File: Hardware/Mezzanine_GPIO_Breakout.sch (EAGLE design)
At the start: 12 parts, among them U2 EDISON_CONNECTOR_FULLMOUNTING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, U3 EDISON_CONNECTOR_FULLHEADER

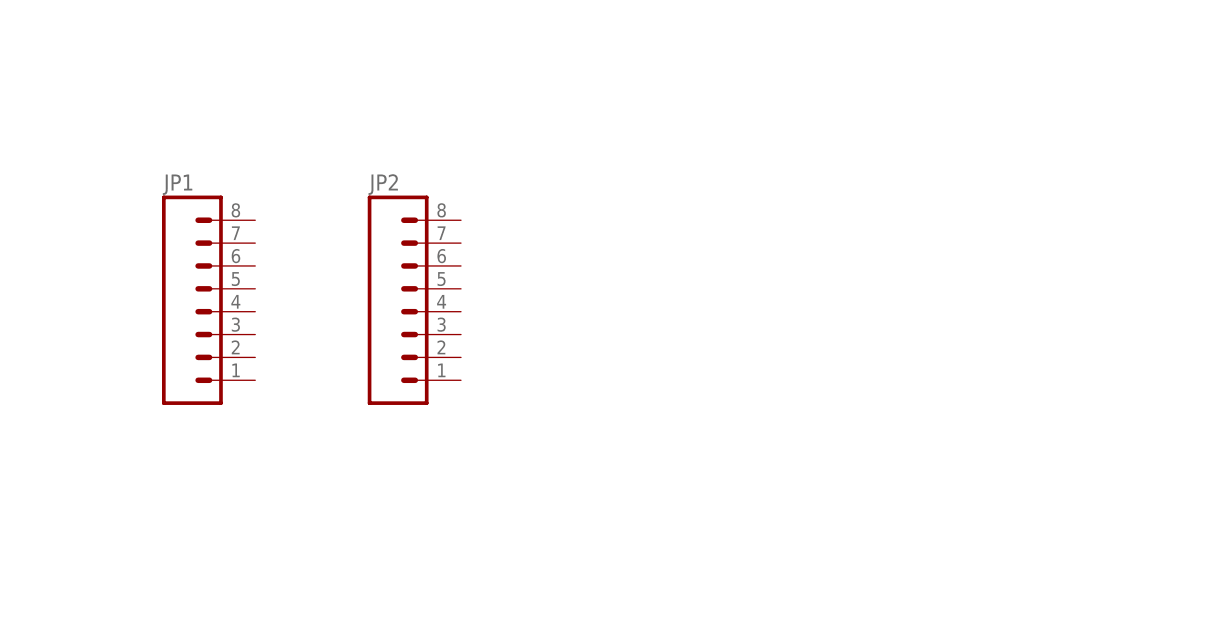
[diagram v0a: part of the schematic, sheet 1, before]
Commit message: completed layout of GPIO Ready for review
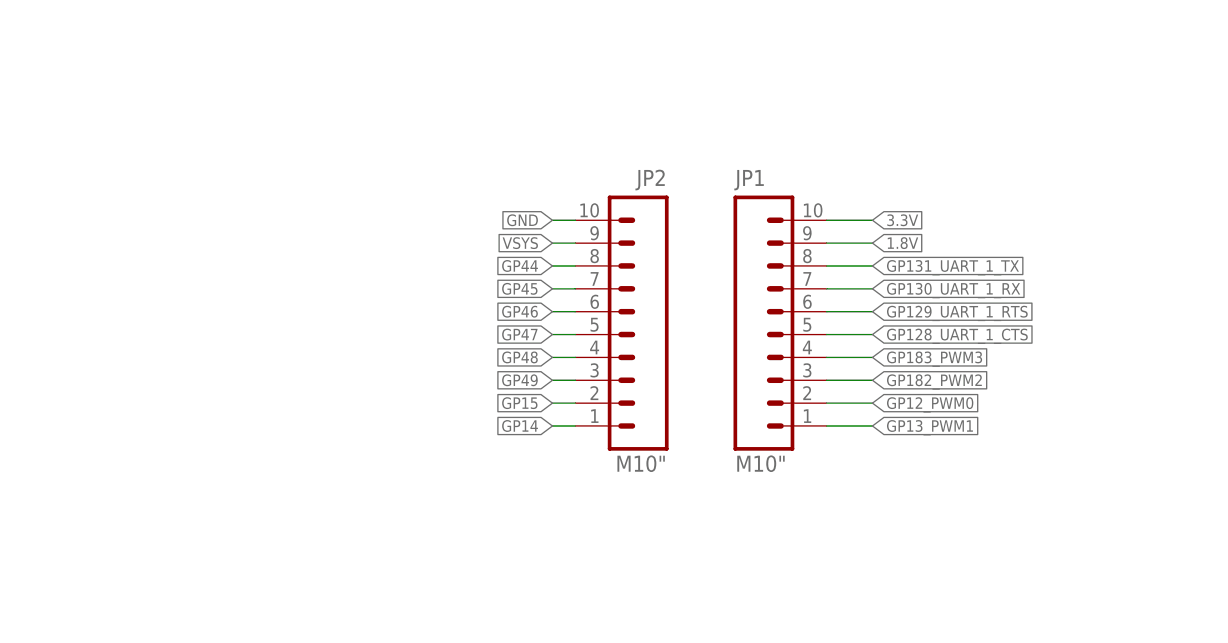
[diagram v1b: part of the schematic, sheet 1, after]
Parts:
- JP1, JP2: value (none) -> M10"; device SparkFun-Connectors:M08 -> SparkFun-Connectors:M10"
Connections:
- net 1.8V: now also JP1.9
- net 3.3V: now also JP1.10
- net GND: now also JP2.10
- net GP128_UART_1_CTS: now also JP1.5
- net GP129_UART_1_RTS: now also JP1.6
- net GP12_PWM0: now also JP1.2
- net GP130_UART_1_RX: now also JP1.7
- net GP131_UART_1_TX: now also JP1.8
- net GP13_PWM1: now also JP1.1
- net GP14: now also JP2.1
- net GP15: now also JP2.2
- net GP182_PWM2: now also JP1.3
- net GP183_PWM3: now also JP1.4
- net GP44: now also JP2.8
- net GP45: now also JP2.7
- net GP46: now also JP2.6
- net GP47: now also JP2.5
- net GP48: now also JP2.4
- net GP49: now also JP2.3
- net VSYS: now also JP2.9
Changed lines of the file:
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@@
 <part name="FID3" library="SparkFun-Aesthetics" deviceset="FIDUCIAL" device="1X2"/>
 <part name="FID4" library="SparkFun-Aesthetics" deviceset="FIDUCIAL" device="1X2"/>
-<part name="JP1" library="SparkFun-Connectors" deviceset="M08" device=""/>
-<part name="JP2" library="SparkFun-Connectors" deviceset="M08" device=""/>
+<part name="JP1" library="SparkFun-Connectors" deviceset="M10" device="&quot;"/>
+<part name="JP2" library="SparkFun-Connectors" deviceset="M10" device="&quot;"/>
 </parts>
 <sheets>
@@
 <instance part="FID3" gate="G$1" x="241.3" y="30.48"/>
 <instance part="FID4" gate="G$1" x="246.38" y="30.48"/>
-<instance part="JP1" gate="G$1" x="68.58" y="101.6"/>
-<instance part="JP2" gate="G$1" x="91.44" y="101.6"/>
+<instance part="JP1" gate="G$1" x="127" y="106.68"/>
+<instance part="JP2" gate="G$1" x="119.38" y="106.68" rot="MR0"/>
 </instances>
 <busses>
 </busses>
 <nets>
+<net name="GP14" class="0">
+<segment>
+<wire x1="109.22" y1="88.9" x2="106.68" y2="88.9" width="0.1524" layer="91"/>
+<label x="106.68" y="88.9" size="1.27" layer="95" rot="R180" xref="yes"/>
+<pinref part="JP2" gate="G$1" pin="1"/>
+</segment>
+</net>
+<net name="GP15" class="0">
+<segment>
+<wire x1="109.22" y1="91.44" x2="106.68" y2="91.44" width="0.1524" layer="91"/>
+<label x="106.68" y="91.44" size="1.27" layer="95" rot="R180" xref="yes"/>
+<pinref part="JP2" gate="G$1" pin="2"/>
+</segment>
+</net>
+<net name="GP49" class="0">
+<segment>
+<wire x1="109.22" y1="93.98" x2="106.68" y2="93.98" width="0.1524" layer="91"/>
+<label x="106.68" y="93.98" size="1.27" layer="95" rot="R180" xref="yes"/>
+<pinref part="JP2" gate="G$1" pin="3"/>
+</segment>
+</net>
+<net name="GP48" class="0">
+<segment>
+<wire x1="109.22" y1="96.52" x2="106.68" y2="96.52" width="0.1524" layer="91"/>
+<label x="106.68" y="96.52" size="1.27" layer="95" rot="R180" xref="yes"/>
+<pinref part="JP2" gate="G$1" pin="4"/>
+</segment>
+</net>
+<net name="GP47" class="0">
+<segment>
+<wire x1="109.22" y1="99.06" x2="106.68" y2="99.06" width="0.1524" layer="91"/>
+<label x="106.68" y="99.06" size="1.27" layer="95" rot="R180" xref="yes"/>
+<pinref part="JP2" gate="G$1" pin="5"/>
+</segment>
+</net>
+<net name="GP46" class="0">
+<segment>
+<wire x1="109.22" y1="101.6" x2="106.68" y2="101.6" width="0.1524" layer="91"/>
+<label x="106.68" y="101.6" size="1.27" layer="95" rot="R180" xref="yes"/>
+<pinref part="JP2" gate="G$1" pin="6"/>
+</segment>
+</net>
+<net name="GP45" class="0">
+<segment>
+<wire x1="109.22" y1="104.14" x2="106.68" y2="104.14" width="0.1524" layer="91"/>
+<label x="106.68" y="104.14" size="1.27" layer="95" rot="R180" xref="yes"/>
+<pinref part="JP2" gate="G$1" pin="7"/>
+</segment>
+</net>
+<net name="GP44" class="0">
+<segment>
+<wire x1="109.22" y1="106.68" x2="106.68" y2="106.68" width="0.1524" layer="91"/>
+<label x="106.68" y="106.68" size="1.27" layer="95" rot="R180" xref="yes"/>
+<pinref part="JP2" gate="G$1" pin="8"/>
+</segment>
+</net>
+<net name="GP183_PWM3" class="0">
+<segment>
+<label x="142.24" y="96.52" size="1.27" layer="95" xref="yes"/>
+<wire x1="137.16" y1="96.52" x2="142.24" y2="96.52" width="0.1524" layer="91"/>
+<pinref part="JP1" gate="G$1" pin="4"/>
+</segment>
+</net>
+<net name="GP182_PWM2" class="0">
+<segment>
+<label x="142.24" y="93.98" size="1.27" layer="95" xref="yes"/>
+<wire x1="137.16" y1="93.98" x2="142.24" y2="93.98" width="0.1524" layer="91"/>
+<pinref part="JP1" gate="G$1" pin="3"/>
+</segment>
+</net>
+<net name="GP13_PWM1" class="0">
+<segment>
+<label x="142.24" y="88.9" size="1.27" layer="95" xref="yes"/>
+<wire x1="137.16" y1="88.9" x2="142.24" y2="88.9" width="0.1524" layer="91"/>
+<pinref part="JP1" gate="G$1" pin="1"/>
+</segment>
+</net>
+<net name="GP12_PWM0" class="0">
+<segment>
+<label x="142.24" y="91.44" size="1.27" layer="95" xref="yes"/>
+<wire x1="137.16" y1="91.44" x2="142.24" y2="91.44" width="0.1524" layer="91"/>
+<pinref part="JP1" gate="G$1" pin="2"/>
+</segment>
+</net>
+<net name="GP131_UART_1_TX" class="0">
+<segment>
+<label x="142.24" y="106.68" size="1.27" layer="95" rot="MR180" xref="yes"/>
+<wire x1="137.16" y1="106.68" x2="142.24" y2="106.68" width="0.1524" layer="91"/>
+<pinref part="JP1" gate="G$1" pin="8"/>
+</segment>
+</net>
+<net name="GP130_UART_1_RX" class="0">
+<segment>
+<label x="142.24" y="104.14" size="1.27" layer="95" rot="MR180" xref="yes"/>
+<wire x1="137.16" y1="104.14" x2="142.24" y2="104.14" width="0.1524" layer="91"/>
+<pinref part="JP1" gate="G$1" pin="7"/>
+</segment>
+</net>
+<net name="GP129_UART_1_RTS" class="0">
+<segment>
+<label x="142.24" y="101.6" size="1.27" layer="95" rot="MR180" xref="yes"/>
+<wire x1="137.16" y1="101.6" x2="142.24" y2="101.6" width="0.1524" layer="91"/>
+<pinref part="JP1" gate="G$1" pin="6"/>
+</segment>
+</net>
+<net name="GP128_UART_1_CTS" class="0">
+<segment>
+<label x="142.24" y="99.06" size="1.27" layer="95" rot="MR180" xref="yes"/>
+<wire x1="137.16" y1="99.06" x2="142.24" y2="99.06" width="0.1524" layer="91"/>
+<pinref part="JP1" gate="G$1" pin="5"/>
+</segment>
+</net>
+<net name="GND" class="0">
+<segment>
+<pinref part="JP2" gate="G$1" pin="10"/>
+<wire x1="109.22" y1="111.76" x2="106.68" y2="111.76" width="0.1524" layer="91"/>
+<label x="106.68" y="111.76" size="1.27" layer="95" rot="R180" xref="yes"/>
+</segment>
+</net>
+<net name="VSYS" class="0">
+<segment>
+<pinref part="JP2" gate="G$1" pin="9"/>
+<wire x1="109.22" y1="109.22" x2="106.68" y2="109.22" width="0.1524" layer="91"/>
+<label x="106.68" y="109.22" size="1.27" layer="95" rot="R180" xref="yes"/>
+</segment>
+</net>
+<net name="3.3V" class="0">
+<segment>
+<label x="142.24" y="111.76" size="1.27" layer="95" xref="yes"/>
+<wire x1="137.16" y1="111.76" x2="142.24" y2="111.76" width="0.1524" layer="91"/>
+<pinref part="JP1" gate="G$1" pin="10"/>
+</segment>
+</net>
+<net name="1.8V" class="0">
+<segment>
+<label x="142.24" y="109.22" size="1.27" layer="95" xref="yes"/>
+<wire x1="137.16" y1="109.22" x2="142.24" y2="109.22" width="0.1524" layer="91"/>
+<pinref part="JP1" gate="G$1" pin="9"/>
+</segment>
+</net>
 </nets>
 </sheet>

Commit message: added rev number to SCH
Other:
- note added: "Casey Kuhns"
- note added: "v01"
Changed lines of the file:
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@@
 <sheet>
 <plain>
+<text x="238.76" y="7.62" size="2.54" layer="94">v01</text>
+<text x="167.64" y="10.16" size="2.54" layer="94">Casey Kuhns</text>
 </plain>
 <instances>
